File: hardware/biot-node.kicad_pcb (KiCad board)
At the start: 2 copper layers, 36.8 x 29 mm, 11 parts, among them J1 MPU9250 connection, J2 3.3V DC, P1 ATSAMR21B, P2 ATSAMR21B-TEST-POINTs, P3 ATMEL-CORTEX, P4 FTDI/Serial, SW1 Reset

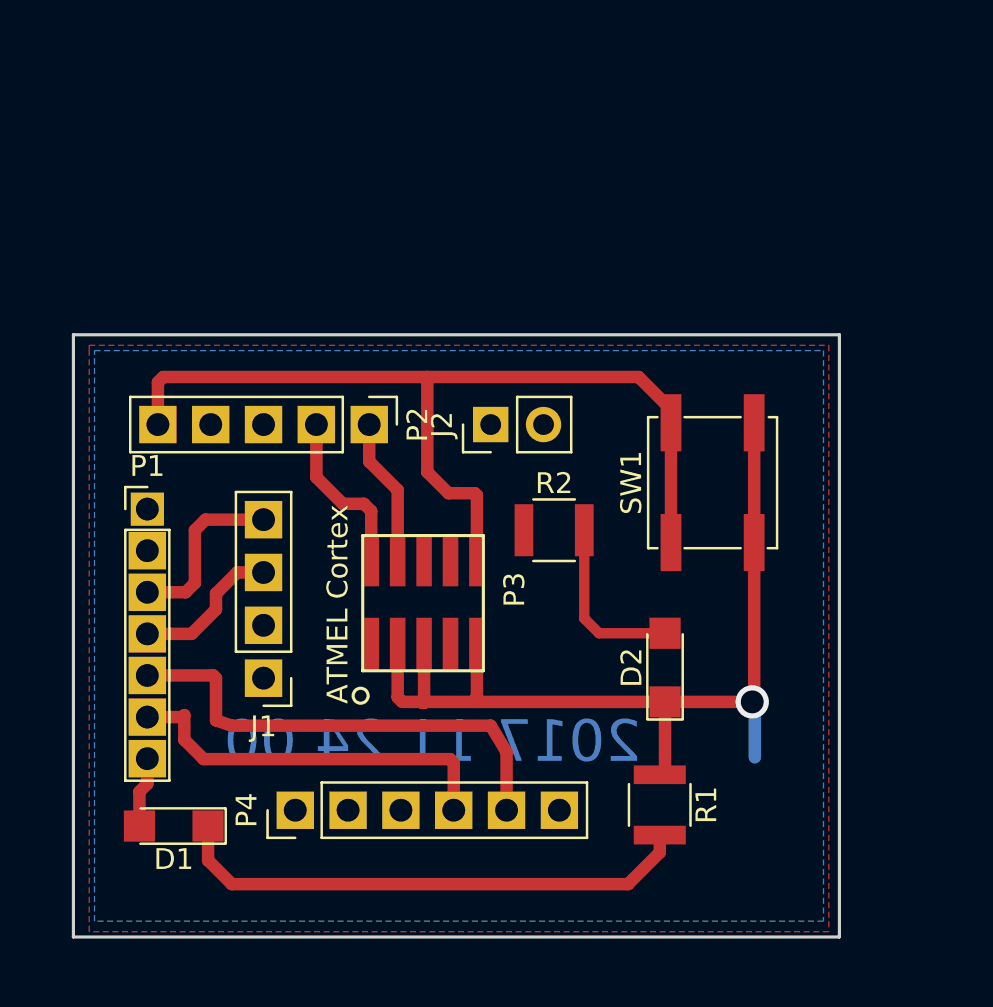
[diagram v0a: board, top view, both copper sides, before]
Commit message: Adding latest biot node circuits.
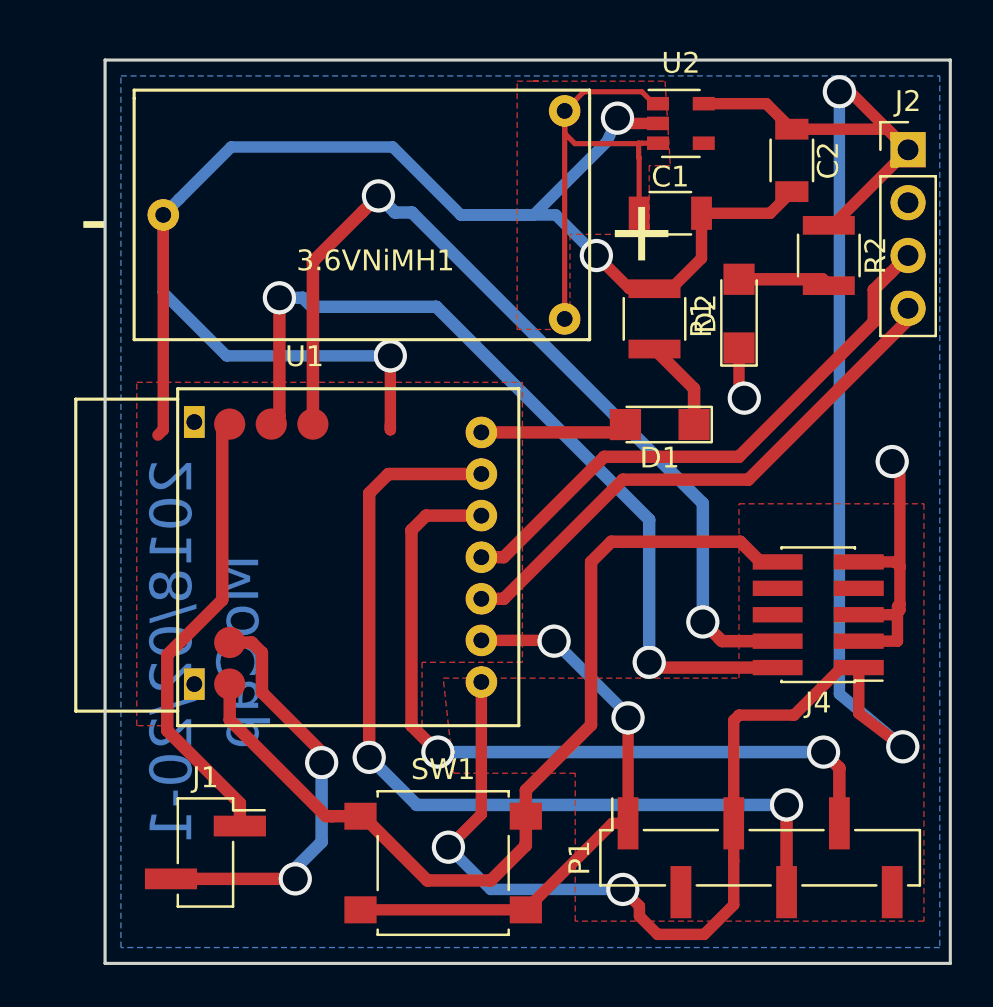
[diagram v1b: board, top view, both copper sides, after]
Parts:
- removed P2: ATSAMR21B-TEST-POINTs, Pin_Headers:Pin_Header_Straight_1x05_Pitch2.54mm
- removed P3: ATMEL-CORTEX, atmelSAM:ATMEL_cortex_header_smd
- removed P4: FTDI/Serial, Pin_Header_Straight_1x06_Pitch2.54mm
- added 3.6VNiMH1: Battery, atsamr21:varta_3V80H_Battery, F.Cu at (187.2, 90.4)
- added C1: 1uF, Capacitors_SMD:C_1206, F.Cu at (192.3, 85.3)
- added C2: 4.7uF, Capacitors_SMD:C_1206, F.Cu at (198.1, 82.8)
- added J4: ATMEL-CORTEX, Pin_Headers:Pin_Header_Straight_2x05_Pitch1.27mm_SMD, F.Cu at (199.4, 104.6)
- added U1: ATSAMR21B18-MZ210PA, atsamr21:ATSAMR21B18-MZ210PA, F.Cu at (164.6, 110.0)
- added U2: LP2985-3.3, TO_SOT_Packages_SMD:SOT-23-5, F.Cu at (192.8, 81.0)
- J1: value MPU9250 connection -> Test Points; footprint Pin_Header_Straight_1x04_Pitch2.54mm -> Pin_Headers:Pin_Header_Straight_1x02_Pitch2.54mm_SMD_Pin1Right
- J2: value 3.3V DC -> MPU9250 connection; footprint Pin_Headers:Pin_Header_Straight_1x02_Pitch2.54mm -> Pin_Headers:Pin_Header_Straight_1x04_Pitch2.54mm
- P1: value ATSAMR21B -> FTDI/Serial; footprint biotx-bits:Pin_Header_Straight_1x07_Pitch2.00mm -> Pin_Headers:Pin_Header_Straight_1x06_Pitch2.54mm_SMD_Pin1Right
- SW1: value Reset -> SW_Reset; footprint Buttons_Switches_SMD:SW_SPST_EVPBF -> Buttons_Switches_SMD:SW_SPST_B3S-1000
- moved P1 33.9 mm to (196.6, 116.3), turned to 90 degrees
- moved D1 30.3 mm to (191.8, 95.5)
- moved J2 24.0 mm to (203.7, 82.3), turned to 0 degrees
- moved R1 23.4 mm to (191.5, 90.4)
- moved SW1 22.4 mm to (181.4, 116.6), turned to 0 degrees
- moved R2 18.7 mm to (199.9, 87.4), turned to 270 degrees
- moved D2 17.4 mm to (195.6, 90.2)
- moved J1 8.84 mm to (169.9, 116.1), turned to 0 degrees
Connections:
- J1 pad 1: +3V3 -> PA14
- J1 pad 2: GND -> PA15
- P1 pad 1: +3V3 -> GND
- P1 pad 2: GND -> Net-(P1-Pad2)
- P1 pad 3: SDA -> +3V3
- P1 pad 4: SCLK -> TX
- P1 pad 6: TX -> Net-(P1-Pad6)
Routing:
- net +3V3: track 0.00 -> 99.2 mm, vias 0 -> 4
- net GND: track 46.3 -> 126.7 mm, vias 1 -> 7
- net SWDCLK: track 7.23 -> 43.7 mm, vias 0 -> 2
- net SWDIO: track 8.35 -> 41.7 mm, vias 0 -> 2
- net TX: track 18.7 -> 43.7 mm, vias 0 -> 2
- net Net-(3.6VNiMH1-Pad1): track 0.00 -> 24.3 mm
- net PA14: track 0.00 -> 22.0 mm
- net Net-(D1-Pad1): track 25.3 -> 4.42 mm
- net PA15: track 0.00 -> 20.3 mm, vias 0 -> 2
- net SCLK: track 7.77 -> 27.4 mm
- net SDA: track 8.52 -> 26.6 mm
- net RX: track 23.4 -> 37.1 mm, vias 0 -> 2
- net Net-(D2-Pad2): track 8.42 -> 4.44 mm
- net Net-(D1-Pad2): track 3.93 -> 7.08 mm
- added copper zone on F.Cu, net GND
- added copper zone on F.Cu, net Net-(3.6VNiMH1-Pad1)
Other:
- board size 36.8 x 29 mm -> 40.6 x 43.4 mm
- net class cnc: via_drill 1.1 -> 1.2
- net class cnc-narrow added: clearance 0.3, trace_width 0.55, via_dia 1.6, via_drill 1.2
- board text added: "2018/02/20-1 MoCap"
- board text removed: "2017 11 24 00"

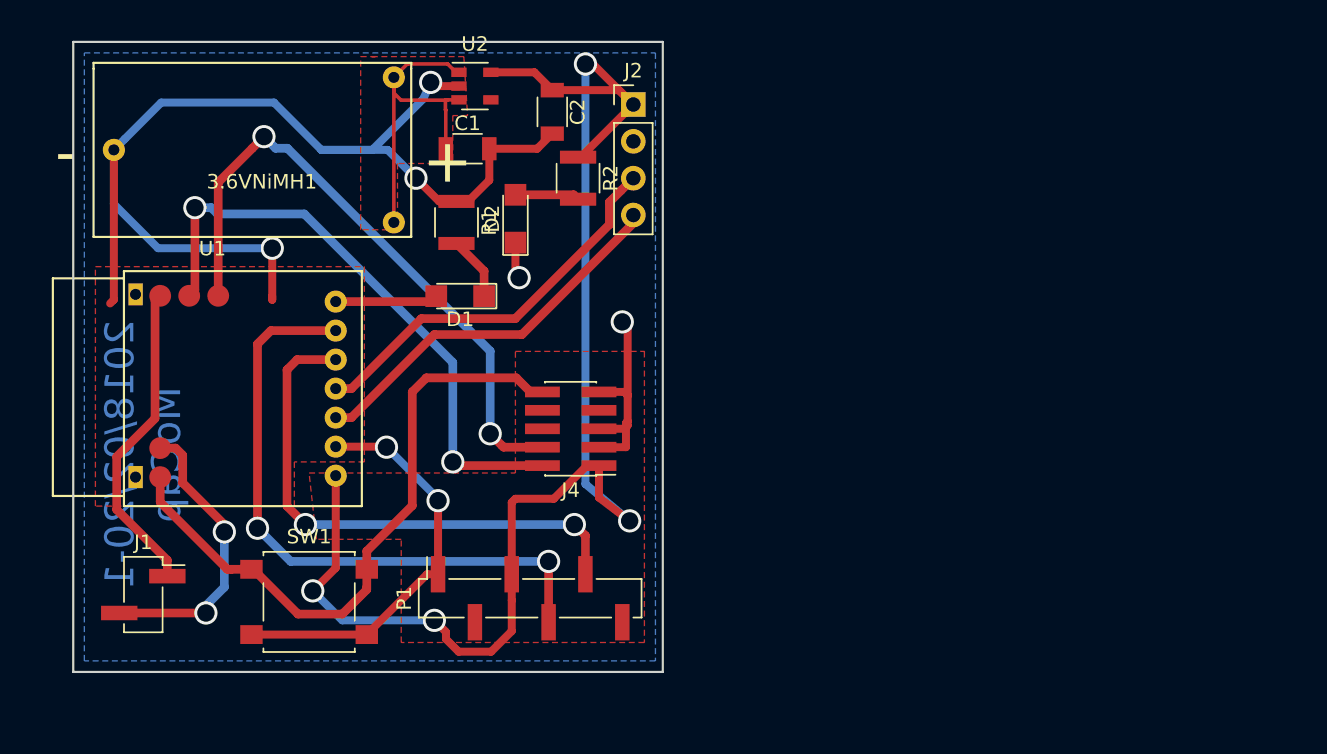
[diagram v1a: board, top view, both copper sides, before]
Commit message: Hardware with CR123 battery holder.
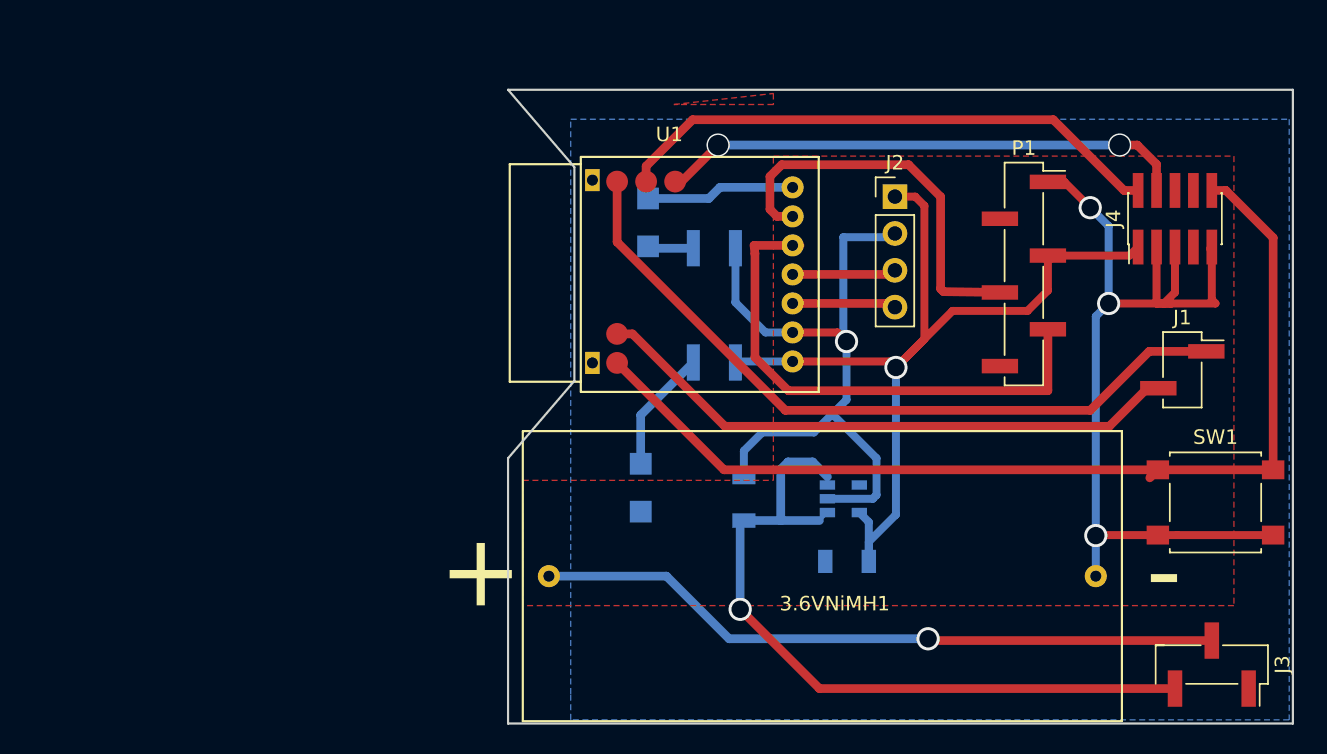
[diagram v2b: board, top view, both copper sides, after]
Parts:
- added J3: on/off, Pin_Headers:Pin_Header_Straight_1x03_Pitch2.54mm_SMD_Pin1Right, F.Cu at (243.6, 120.9)
- 3.6VNiMH1: footprint atsamr21:varta_3V80H_Battery -> atsamr21:CR123_Battery_Holder
- C1, C2, D1, D2, R1, R2, U2: moved to B.Cu
- moved J1 73.3 mm to (241.6, 100.6)
- moved SW1 62.9 mm to (243.8, 109.7)
- moved J4 44.1 mm to (241.0, 90.2), turned to 90 degrees
- moved P1 40.7 mm to (230.6, 94.0), turned to 0 degrees
- moved U2 38.1 mm to (218.2, 109.5)
- moved C2 37.1 mm to (218.4, 113.8), turned to 180 degrees
- moved U1 32.5 mm to (196.1, 102.1)
- moved C1 30.7 mm to (211.3, 109.5), turned to 90 degrees
- moved 3.6VNiMH1 26.0 mm to (196.1, 114.8), turned to 0 degrees
- moved D2 20.5 mm to (204.2, 108.7)
- moved J2 19.1 mm to (221.7, 88.6)
- moved R1 17.9 mm to (209.3, 92.2), turned to 180 degrees
- moved R2 15.8 mm to (209.3, 100.1), turned to 180 degrees
- moved D1 13.9 mm to (204.7, 90.4), turned to 90 degrees
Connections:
- C1 pad 1: Net-(3.6VNiMH1-Pad1) -> Net-(C1-Pad1)
- U2 pad 1: Net-(3.6VNiMH1-Pad1) -> Net-(C1-Pad1)
- U2 pad 3: Net-(3.6VNiMH1-Pad1) -> Net-(C1-Pad1)
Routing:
- net Net-(C1-Pad1): track 0.00 -> 52.6 mm, vias 0 -> 1
- net +3V3: track 99.2 -> 65.1 mm, vias 4 -> 1
- net PA14: track 22.0 -> 51.3 mm
- net NRST: track 44.6 -> 70.6 mm
- net Net-(3.6VNiMH1-Pad1): track 24.3 -> 47.8 mm, vias 0 -> 1
- net PA15: track 20.3 -> 41.0 mm, vias 2 -> 0
- net SCLK: track 27.4 -> 7.17 mm
- net SDA: track 26.6 -> 7.16 mm
- net TX: track 43.7 -> 27.6 mm, vias 2 -> 0
- net GND: track 126.7 -> 111.7 mm, vias 7 -> 4
- net SWDCLK: track 43.7 -> 36.6 mm
- net Net-(D2-Pad2): track 4.44 -> 8.49 mm
- net SWDIO: track 41.7 -> 38.3 mm, vias 2 -> 0
- net Net-(D1-Pad2): track 7.08 -> 10.3 mm
- net Net-(D1-Pad1): track 4.42 -> 3.18 mm
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- removed copper zone on F.Cu, net GND
- removed copper zone on F.Cu, net Net-(3.6VNiMH1-Pad1)
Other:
- board size 40.6 x 43.4 mm -> 54.1 x 43.7 mm
- net class cnc: via_drill 1.2 -> 1.4
- board text removed: "2018/02/20-1 MoCap"

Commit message: Newer node hardware construction.
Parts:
- added REF**: Pin_Header_Straight_1x01_Pitch1.00mm, Pin_Headers:Pin_Header_Straight_1x01_Pitch1.00mm, F.Cu at (132.3, 99.1)
- added REF**: Pin_Header_Straight_1x01_Pitch1.00mm, Pin_Headers:Pin_Header_Straight_1x01_Pitch1.00mm, F.Cu at (133.3, 53.8)
- 3.6VNiMH1: footprint atsamr21:CR123_Battery_Holder -> atsamr21:varta3v200h
- D1: value SIGNAL -> 20mA
- D2: value PWR -> 20mA
- J1: value Test Points -> test points; footprint Pin_Headers:Pin_Header_Straight_1x02_Pitch2.54mm_SMD_Pin1Right -> Pin_Headers:Pin_Header_Straight_1x03_Pitch2.54mm_SMD_Pin1Right
- R1, R2: value 39 -> 68
- moved J3 126.7 mm to (118.1, 103.4), turned to 90 degrees
- moved J1 123.4 mm to (118.4, 94.0), turned to 90 degrees
- moved P1 110.8 mm to (125.7, 58.4), turned to 270 degrees
- moved SW1 109.3 mm to (143.0, 67.6), turned to 180 degrees
- moved J4 96.2 mm to (145.8, 76.7)
- moved U2 88.0 mm to (133.1, 86.9)
- moved C1 86.3 mm to (128.0, 86.9)
- moved D2 86.3 mm to (120.9, 86.1)
- moved R1 86.3 mm to (126.0, 69.6)
- moved R2 86.3 mm to (126.0, 77.5)
- moved U1 86.3 mm to (112.8, 79.5)
- moved D1 86.3 mm to (121.4, 67.8)
- moved C2 85.6 mm to (135.4, 93.2)
- moved J2 80.1 mm to (149.4, 54.4)
- moved 3.6VNiMH1 54.6 mm to (150.6, 84.6), turned to 180 degrees
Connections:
- J1 pad 2: PA15 -> GND
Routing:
- net +3V3: track 65.1 -> 113.9 mm, vias 1 -> 2
- net RX: track 36.3 -> 13.9 mm
- net Net-(3.6VNiMH1-Pad1): track 47.8 -> 25.9 mm, vias 1 -> 0
- net GND: track 111.7 -> 133.5 mm, vias 4 -> 2
- net PA14: track 51.3 -> 30.1 mm
- net Net-(C1-Pad1): track 52.6 -> 32.4 mm
- net SDA: track 7.16 -> 27.0 mm
- net PA15: track 41.0 -> 21.8 mm
- net SCLK: track 7.17 -> 25.7 mm
- net TX: track 27.6 -> 13.9 mm
- net NRST: track 70.6 -> 62.7 mm
- net SWDIO: track 38.3 -> 36.4 mm
- net SWDCLK: track 36.6 -> 37.7 mm, vias 2 -> 0
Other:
- board size 54.1 x 43.7 mm -> 41.7 x 58.7 mm
- net class Default: clearance 0.2 -> 0.15
- net class cnc: via_dia 1.6 -> 1.8
- net class cnc-narrow: clearance 0.3 -> 0.2; via_dia 1.6 -> 1.8; via_drill 1.2 -> 1.4
- rule trace_clearance: 0.2 -> 0.15
- board text added: "Motion Capture 2018-03-15-0"
